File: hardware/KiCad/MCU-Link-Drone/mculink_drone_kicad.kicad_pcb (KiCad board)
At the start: 2 copper layers, 57.9 x 43.1 mm, 111 parts, among them J1 Conn_01x10, J2 Pixhawk_Debug_Mini, J3 Jumper_2_Open, J4 Jumper_2_Open, J5 Jumper_2_Open, J6 Conn_02x05_Odd_Even, J7 1x3pos, 100mil pitch, J9 USB4110-GF-A_REVB, SW1 KMR221GLFS, U1 LPC55S69JBD64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

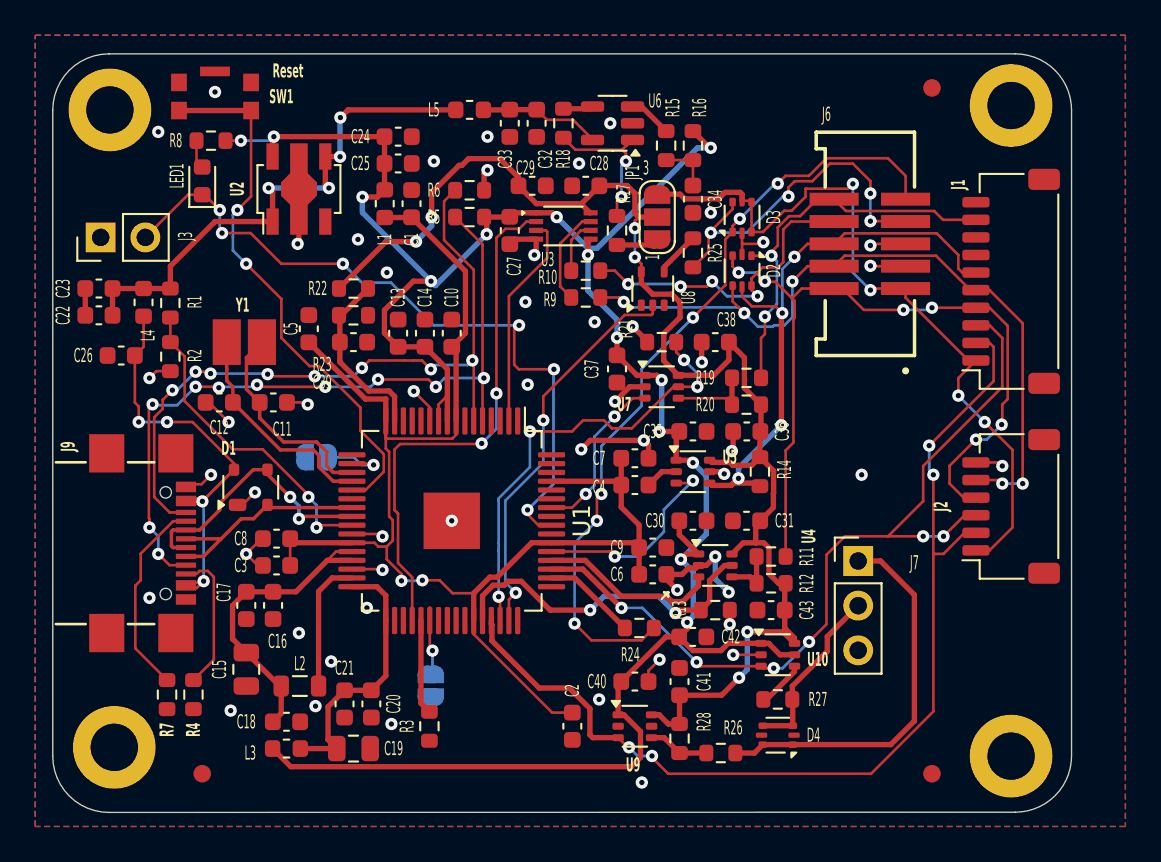
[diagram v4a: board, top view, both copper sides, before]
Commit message: fixed warnings
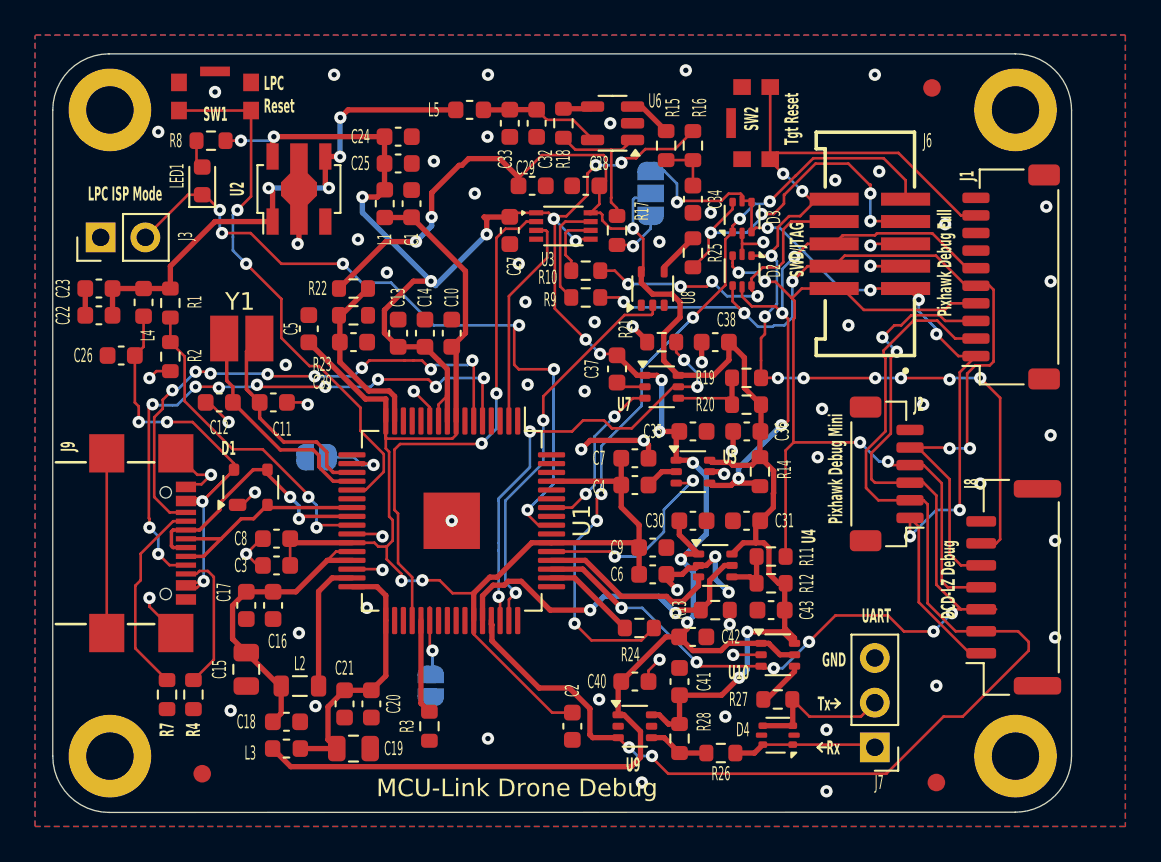
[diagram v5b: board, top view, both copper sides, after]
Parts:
- removed L7: Logo HSLU, McuOnEclipse:Hochschule_Luzern_Small
- removed R5, R6: 100k, Resistor_SMD:R_0603_1608Metric
- added J8: DCD-LZ_Debug, McuOnEclipse:JST_GH_SM07B-GHS-TB_1x07-1MP_P1.25mm_Horizontal, F.Cu at (218.7, 106.4)
- added SW2: KMR221GLFS, McuOnEclipse:SW_C_K_KMR2, F.Cu at (204.0, 80.0)
- J1: value Conn_01x10 -> Pixhawk Debug Full
- J2: footprint McuOnEclipse:JST_SH_SM06B-SRSS-TB_1x06-1MP_P1.00mm_Horizontal -> McuOnEclipse:JST_SH_BM06B-SRSS-TB_1x06-1MP_P1.00mm_Vertical
- JP1: footprint Jumper:SolderJumper-3_P1.3mm_Open_RoundedPad1.0x1.5mm_NumberLabels -> McuOnEclipse:SolderJumper-3_P1.3mm_Open_RoundedPad1.0x1.5mm; moved to B.Cu
- moved J7 10.6 mm to (210.8, 115.5), turned to 180 degrees
- moved J2 7.31 mm to (211.4, 100.0)
- moved L6 3.13 mm to (192.4, 82.4)
- moved JP1 1.40 mm to (198.0, 84.0)
- moved FID2 0.56 mm to (214.2, 117.5)
- moved H3 0.56 mm to (167.2, 116.0)
- moved H2 0.35 mm to (218.8, 79.2)
- moved Y1 0.25 mm to (174.8, 92.2)
- moved H4 0.25 mm to (218.8, 116.0)
- moved J1 0.25 mm to (218.5, 88.8)
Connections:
- J9 pad S1: unconnected-(J9-SHIELD-PadS1)_0 -> GND
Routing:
- net /Debug interface/IF_RST: track 23.0 -> 59.8 mm, vias 2 -> 10
- net Net-(D4A-K1): track 22.1 -> 8.19 mm
- net FC0_TARGET_RXD: track 58.9 -> 70.3 mm, vias 4 -> 2
- net LPC_SWDCLK: track 41.2 -> 30.6 mm
- net GND: track 55.7 -> 65.9 mm, vias 52 -> 71
- net LPC_SWDIO: track 43.0 -> 33.2 mm
- net /Debug interface/IF_SWCLK: track 42.7 -> 51.5 mm
- net FCO_TARGET_TXD: track 49.0 -> 56.4 mm, vias 6 -> 8
- net /Debug interface/VTARGET: track 43.8 -> 49.4 mm, vias 4 -> 7
- net IF_VREF: track 79.9 -> 83.8 mm, vias 6 -> 5
- net +3V3: track 129.2 -> 131.2 mm, vias 14 -> 16
- net /Debug interface/IF_SWDIO: track 46.5 -> 48.4 mm, vias 6 -> 4
- net Net-(D4B-K2): track 10.2 -> 8.69 mm
- net Net-(U3-2B): track 3.07 -> 3.77 mm
- net Net-(JP1-A): track 2.40 -> 3.05 mm, vias 0 -> 1
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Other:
- board text added: "DCD-LZ Debug"
- board text added: "GND"
- board text added: "LPC ISP Mode"
- board text added: "LPC Reset"
- board text added: "MCU-Link Drone Debug"
- board text added: "Pixhawk Debug Full"
- board text added: "Pixhawk Debug Mini"
- board text added: "Rx"
- board text added: "SWD disable"
- board text added: "SWD/JTAG"
- board text added: "Tgt Reset"
- board text added: "Tx"
- board text added: "UART"
- board text added: "VCOM disable"
- board text removed: "Reset"

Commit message: optimized layout
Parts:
- removed R25: 10R, Resistor_SMD:R_0603_1608Metric
- removed U8: 74LVC1G07, Package_TO_SOT_SMD:SOT-353_SC-70-5
- L6: moved to F.Cu
- moved L6 205.4 mm to (4.15, 0.25), turned to 0 degrees
- moved SW1 10.4 mm to (174.4, 88.8)
- moved J5 5.77 mm to (184.5, 97.2), turned to -90 degrees
- moved Y1 3.04 mm to (175.5, 95.2)
- moved C11 2.45 mm to (178.4, 97.5)
- moved C12 2.45 mm to (175.3, 97.5)
- moved J1 2.06 mm to (218.7, 90.8)
- moved H1 1.95 mm to (167.2, 81.2)
- moved H2 1.95 mm to (218.8, 81.2)
- moved FID3 1.90 mm to (214.6, 79.8)
- moved SW2 1.80 mm to (203.9, 81.8), turned to 0 degrees
- moved J2 1.35 mm to (211.4, 101.3)
- moved J8 1.22 mm to (218.8, 105.2)
- moved FID1 1.20 mm to (172.5, 115.8)
- moved H3 1.20 mm to (167.2, 114.8)
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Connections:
- D3 pad 6: /Debug interface/IF_ISPEN -> /Debug interface/VTARGET
- J6 pad 7: /Debug interface/IF_ISPEN -> unconnected-(J6-Pin_7-Pad7)
- U1 pad 47: DBGIF_ISP_CTRL -> unconnected-(U1C-PIO0_14-Pad47)
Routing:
- net DBGIF_ISP_CTRL: track 22.7 -> 0.00 mm, vias 2 -> 0
- net /Debug interface/IF_ISPEN: track 21.5 -> 0.00 mm, vias 4 -> 0
- net /Debug interface/VTARGET: track 49.4 -> 65.6 mm, vias 7 -> 9
- net GND: track 65.9 -> 52.7 mm, vias 71 -> 55
- net LPC_RST: track 31.2 -> 20.8 mm, vias 2 -> 0
- net FC0_TARGET_RXD: track 70.3 -> 60.8 mm, vias 2 -> 4
- net LPC_SWDIO: track 33.2 -> 41.5 mm, vias 10 -> 7
- net /Debug interface/IF_SWCLK: track 51.5 -> 44.3 mm
- net LPC_SWDCLK: track 30.6 -> 37.6 mm, vias 8 -> 4
- net FCO_TARGET_TXD: track 56.4 -> 50.5 mm, vias 8 -> 6
- net /Debug interface/IF_RST: track 59.8 -> 54.0 mm, vias 10 -> 6
- net /Debug interface/IF_SWDIO: track 48.4 -> 53.7 mm, vias 4 -> 8
- net /McuLink Power and USB/Q-: track 12.6 -> 7.74 mm
- net /McuLink Power and USB/Q+: track 13.4 -> 10.2 mm
- net Net-(U1B-USB1_VBUS): track 18.5 -> 21.5 mm
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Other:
- board size 57.9 x 43.1 mm -> 57.9 x 39.9 mm
- board text added: "MCU-Link MR"
- board text removed: "MCU-Link Drone Debug"

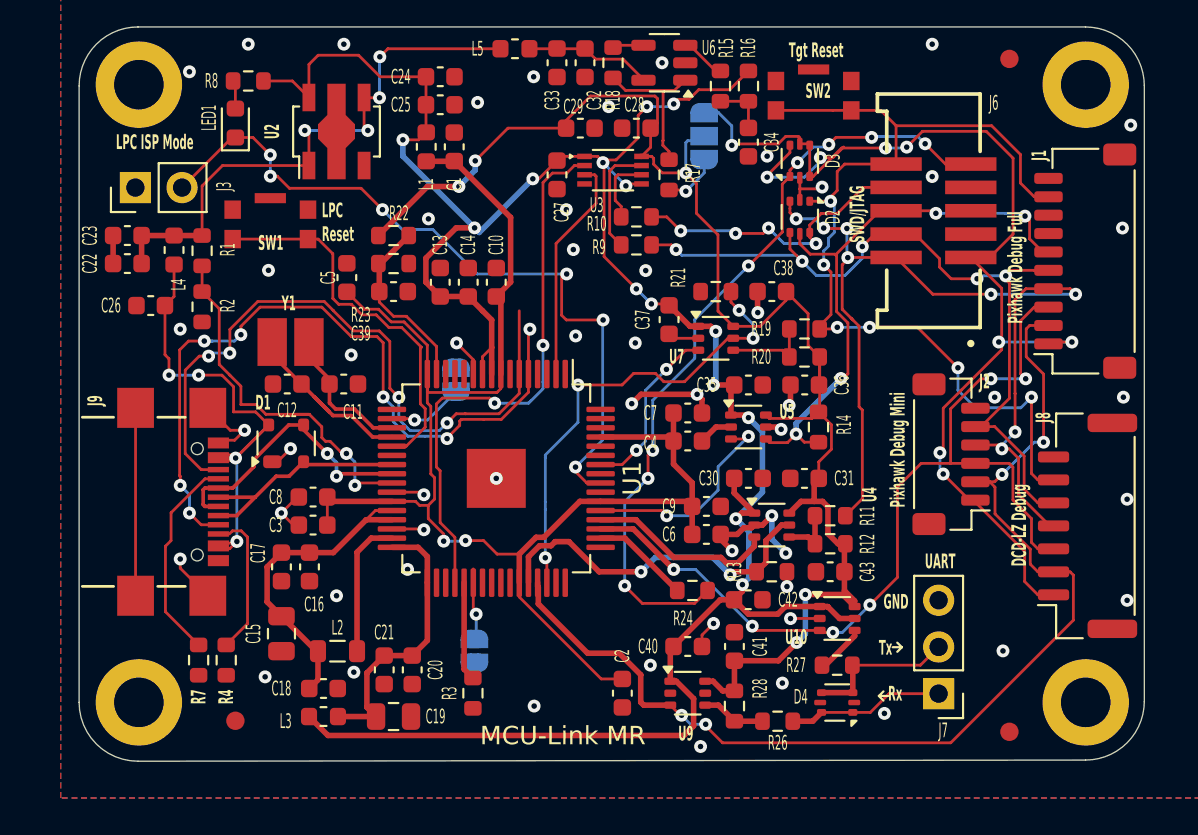
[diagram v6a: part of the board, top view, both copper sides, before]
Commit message: optimized traces
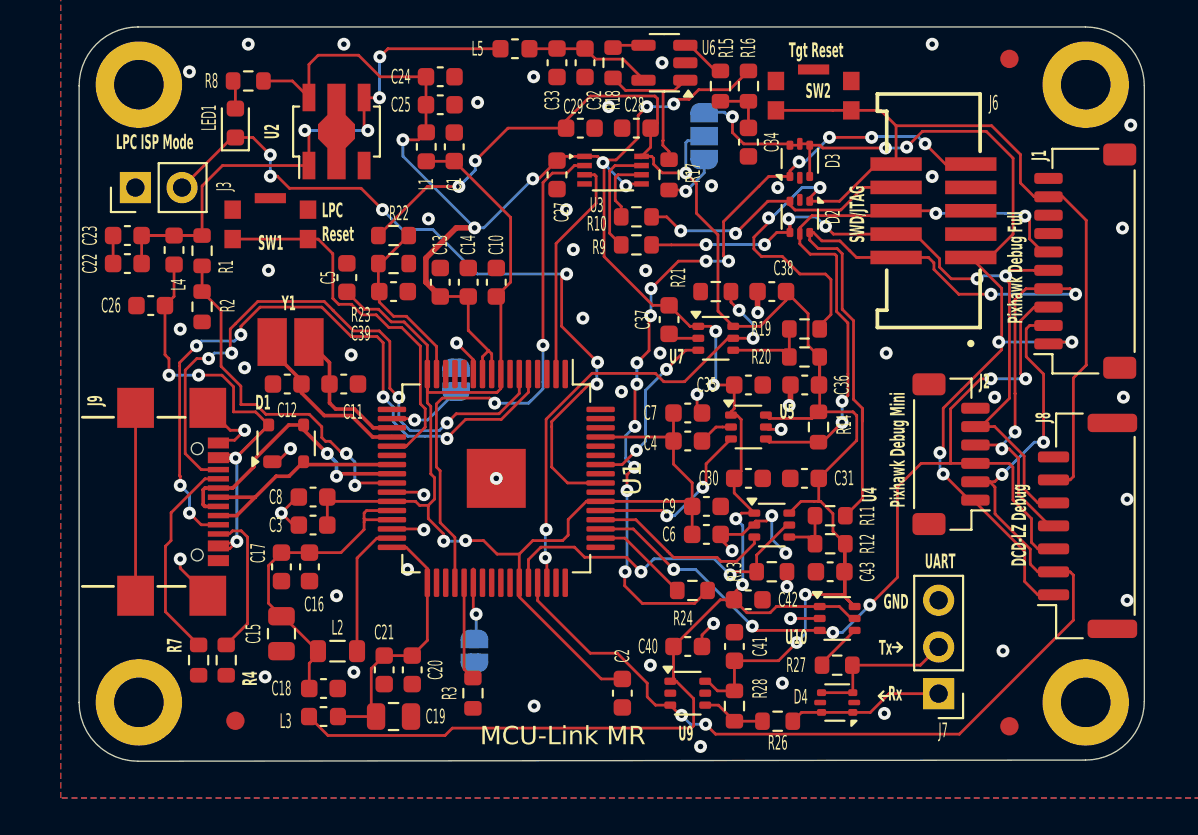
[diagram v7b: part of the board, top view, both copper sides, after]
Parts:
- moved FID2 0.30 mm to (214.6, 116.1)
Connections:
- D2 pad 3: /Debug interface/IF_SWDIO -> /Debug interface/IF_TDI
- D2 pad 6: /Debug interface/IF_TDI -> /Debug interface/IF_SWDIO
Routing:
- net /Debug interface/VTARGET: track 65.6 -> 56.9 mm, vias 9 -> 7
- net GND: track 52.7 -> 46.5 mm, vias 55 -> 57
- net IF_VREF: track 81.0 -> 86.5 mm
- net +3V3: track 131.8 -> 127.7 mm, vias 14 -> 11
- net /Debug interface/IF_RST: track 54.0 -> 57.9 mm, vias 6 -> 2
- net LPC_SWDIO: track 41.5 -> 38.0 mm, vias 7 -> 6
- net LPC_SWDCLK: track 37.6 -> 34.3 mm
- net +5V: track 30.9 -> 34.2 mm
- net /Debug interface/IF_DETECT: track 42.7 -> 45.6 mm, vias 8 -> 14
- net DBGIF_TDO_SWO: track 11.7 -> 9.59 mm
- net Net-(U1B-USB1_VBUS): track 21.5 -> 19.6 mm
- net /Debug interface/IF_SWCLK: track 44.3 -> 42.8 mm, vias 5 -> 6
- net PIO0_5-ISP_EN-LED1_CTRL: track 41.2 -> 42.4 mm
- net /Debug interface/IF_TDI: track 16.5 -> 15.2 mm, vias 4 -> 2
- net /Debug interface/IF_SWO: track 31.4 -> 32.7 mm
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
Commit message: optimized layout
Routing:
- net GND: track 46.5 -> 45.3 mm, vias 57 -> 58
- net FCO_TARGET_TXD: track 50.4 -> 51.5 mm
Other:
- board text added: "Ref V tracking Default: 1-2 closed"
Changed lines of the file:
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@@
 		(tags "solder jumper open")
 		(property "Reference" "J4"
-			(at -2.545 0.0115 -90)
+			(at -2.3 -0.08 0)
 			(layer "B.SilkS")
 			(effects
@@
 		(tags "solder jumper open")
 		(property "Reference" "JP1"
-			(at 0 1.8 270)
+			(at 2.7 0 0)
 			(layer "B.SilkS")
 			(effects
@@
 		(layer "Edge.Cuts")
 	)
+	(gr_text "Ref V tracking\nDefault:\n1-2 closed"
+		(at 203.8 85.8 -0)
+		(layer "B.SilkS")
+		(effects
+			(font
+				(size 0.8 0.4)
+				(thickness 0.08)
+				(bold yes)
+			)
+			(justify left bottom mirror)
+		)
+	)
 	(gr_text "SWD\ndisable"
 		(at 184.5 95.5 0)
@@
 	)
 	(gr_text "VCOM\ndisable"
-		(at 187 112 -90)
+		(at 188 113 0)
 		(layer "B.SilkS")
 		(effects
 			(font
-				(size 1 1)
-				(thickness 0.125)
+				(size 0.8 0.4)
+				(thickness 0.1)
+				(bold yes)
 			)
 			(justify bottom mirror)
@@
 	)
 	(segment
-		(start 200.901 92.456)
-		(end 200.901 93.586)
-		(width 0.3048)
-		(layer "F.Cu")
-		(net 1)
-	)
-	(segment
 		(start 198.641 99.822)
 		(end 199 99.822)
@@
 		(net 1)
 	)
-	(segment
-		(start 200.901 93.586)
-		(end 200.914 93.599)
-		(width 0.3048)
-		(layer "F.Cu")
-		(net 1)
-	)
 	(via
 		(at 178.8 95.9)
@@
 	)
 	(via
+		(at 196.7 91.9)
+		(size 0.7)
+		(drill 0.3)
+		(layers "F.Cu" "B.Cu")
+		(net 1)
+	)
+	(via
 		(at 188.75 115)
 		(size 0.7)
@@
 	)
 	(via
-		(at 200.914 93.599)
+		(at 200.9 91.3)
 		(size 0.7)
 		(drill 0.3)
@@
 	)
 	(segment
-		(start 180.538698 98.189222)
-		(end 180.549476 98.2)
+		(start 169.4666 96.322692)
+		(end 169.4666 102.4666)
 		(width 0.1524)
 		(layer "F.Cu")
@@
 	)
 	(segment
-		(start 184.0118 100.418264)
-		(end 184.0118 100.452185)
+		(start 169.5 102.5)
+		(end 169.5 103)
 		(width 0.1524)
 		(layer "F.Cu")
@@
 	)
 	(segment
-		(start 169.5 102.5)
-		(end 169.4666 102.4666)
+		(start 180.538698 98.189222)
+		(end 180.549476 98.2)
 		(width 0.1524)
 		(layer "F.Cu")
@@
 	)
 	(segment
-		(start 177.2 93.3)
-		(end 178.8 94.9)
+		(start 170.9 95.2)
+		(end 170.589292 95.2)
 		(width 0.1524)
 		(layer "F.Cu")
@@
 	)
 	(segment
-		(start 171.575 105.14)
-		(end 170.64 105.14)
+		(start 184.0118 100.418264)
+		(end 184.0118 100.452185)
 		(width 0.1524)
 		(layer "F.Cu")
@@
 	)
 	(segment
-		(start 178.8 94.9)
-		(end 180.2 94.9)
+		(start 177.2 93.3)
+		(end 178.8 94.9)
 		(width 0.1524)
 		(layer "F.Cu")
@@
 	)
 	(segment
-		(start 169.4666 96.322692)
-		(end 169.4666 96.5)
+		(start 171.575 105.14)
+		(end 170.64 105.14)
 		(width 0.1524)
 		(layer "F.Cu")
@@
 	)
 	(segment
-		(start 172.8 94.3428)
-		(end 173.8428 93.3)
+		(start 169.4666 102.4666)
+		(end 169.5 102.5)
 		(width 0.1524)
 		(layer "F.Cu")
@@
 	)
 	(segment
-		(start 170.381631 95.407661)
-		(end 169.4666 96.322692)
+		(start 178.8 94.9)
+		(end 180.2 94.9)
 		(width 0.1524)
 		(layer "F.Cu")
@@
 	)
 	(segment
-		(start 173.8428 93.3)
-		(end 177.2 93.3)
+		(start 172.8 94.3428)
+		(end 173.8428 93.3)
 		(width 0.1524)
 		(layer "F.Cu")
@@
 	)
 	(segment
-		(start 169.4666 102.4666)
-		(end 169.4666 96.5)
+		(start 173.8428 93.3)
+		(end 177.2 93.3)
 		(width 0.1524)
 		(layer "F.Cu")
@@
 	)
 	(segment
-		(start 169.5 103)
-		(end 169.5 102.5)
+		(start 170.64 105.14)
+		(end 170 104.5)
 		(width 0.1524)
 		(layer "F.Cu")
@@
 	)
 	(segment
-		(start 170.64 105.14)
-		(end 170 104.5)
+		(start 172.8 94.8)
+		(end 172.8 94.3428)
 		(width 0.1524)
 		(layer "F.Cu")
@@
 	)
 	(segment
-		(start 172.8 94.8)
-		(end 172.8 94.3428)
+		(start 170.589292 95.2)
+		(end 169.4666 96.322692)
 		(width 0.1524)
 		(layer "F.Cu")
@@
 	)
 	(via
-		(at 170.381631 95.407661)
+		(at 170.9 95.2)
 		(size 0.7)
 		(drill 0.3)
@@
 	)
 	(segment
-		(start 170.642533 95.146759)
-		(end 170.381631 95.407661)
-		(width 0.1524)
-		(layer "B.Cu")
-		(net 28)
-	)
-	(segment
 		(start 170 103.5)
 		(end 170 104.5)
@@
 	)
 	(segment
+		(start 172.4 95.2)
+		(end 172.8 94.8)
+		(width 0.1524)
+		(layer "B.Cu")
+		(net 28)
+	)
+	(segment
 		(start 184.0118 100.452185)
 		(end 183.884015 100.3244)
@@
 	)
 	(segment
-		(start 182.8 100.3244)
-		(end 181.879084 100.3244)
+		(start 170.9 95.2)
+		(end 172.4 95.2)
 		(width 0.1524)
 		(layer "B.Cu")
@@
 	)
 	(segment
-		(start 172.453241 95.146759)
-		(end 170.642533 95.146759)
-		(width 0.1524)
-		(layer "B.Cu")
-		(net 28)
-	)
-	(segment
-		(start 172.453241 95.146759)
-		(end 172.8 94.8)
+		(start 182.8 100.3244)
+		(end 181.879084 100.3244)
 		(width 0.1524)
 		(layer "B.Cu")
@@
 	)
 	(segment
+		(start 196.342 107.569)
+		(end 198.2 107.569)
+		(width 0.1524)
+		(layer "F.Cu")
+		(net 50)
+	)
+	(segment
 		(start 204.396 111)
 		(end 204.282 110.886)
@@
 	)
 	(segment
-		(start 208.509871 108)
-		(end 207.009399 109.500472)
+		(start 208.509871 109.590129)
+		(end 207.1 111)
 		(width 0.1524)
 		(layer "F.Cu")
@@
 	)
 	(segment
+		(start 208.509871 108)
+		(end 208.509871 109.590129)
+		(width 0.1524)
+		(layer "F.Cu")
+		(net 50)
+	)
+	(segment
 		(start 214.7904 103.7904)
 		(end 215.8 104.8)
@@
 	)
 	(segment
-		(start 207.009399 109.500472)
-		(end 207.168471 109.3414)
-		(width 0.1524)
-		(layer "F.Cu")
-		(net 50)
-	)
-	(segment
-		(start 207.000472 109.500472)
-		(end 207.009399 109.500472)
-		(width 0.1524)
-		(layer "F.Cu")
-		(net 50)
-	)
-	(segment
-		(start 207 109.5)
-		(end 207.000472 109.500472)
-		(width 0.1524)
-		(layer "F.Cu")
-		(net 50)
-	)
-	(segment
 		(start 216.150001 106.45)
 		(end 217 106.45)
@@
 	)
 	(via
-		(at 207.009399 109.500472)
+		(at 207.1 111)
 		(size 0.7)
 		(drill 0.3)
@@
 	)
 	(via
-		(at 196.342 107.569)
+		(at 198.2 107.569)
 		(size 0.7)
 		(drill 0.3)
@@
 	)
 	(segment
-		(start 200.614519 110.654969)
-		(end 197.52855 107.569)
+		(start 198.2 107.569)
+		(end 200.614519 109.983519)
 		(width 0.1524)
 		(layer "B.Cu")
@@
 	)
 	(segment
-		(start 197.52855 107.569)
-		(end 196.342 107.569)
-		(width 0.1524)
-		(layer "B.Cu")
-		(net 50)
-	)
-	(segment
-		(start 207.009399 109.500472)
-		(end 205.509871 111)
+		(start 205 111)
+		(end 207.1 111)
 		(width 0.1524)
 		(layer "B.Cu")
@@
 	)
 	(segment
-		(start 205.509871 111)
-		(end 205 111)
+		(start 200.614519 109.983519)
+		(end 200.614519 110.654969)
 		(width 0.1524)
 		(layer "B.Cu")
